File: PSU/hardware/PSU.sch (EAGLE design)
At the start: 211 parts, among them J1 SWD, J2 UART, Q1 PMOS-DPAK, Q10 PMOS-SOT23, Q11 NPN, Q12 PMOS-SOT23, Q13 NPN, Q14 NPN, Q15 PMOS-SOT23, Q2 PMOS-SOT23, Q3 NPN, Q4 PMOS-SOT23, Q5 NMOS-SOT23, Q6 PMOS-DPAK, Q7 PMOS-SOT23, Q8 NMOS-SOT23, Q9 PMOS-DPAK, U1 LM2576, U10 4069, U11 LTV-247, U12 74HC08, U13 STM8S003K3T6C, U14 74HC08, U15 4051, U16 358, U17 358, U18 74HC32, U2 MT3608, U3 7805, U4 324, U5 MC34063, U6 MT3608, U7 LM2576, U8 MC34063, U9 TP4056

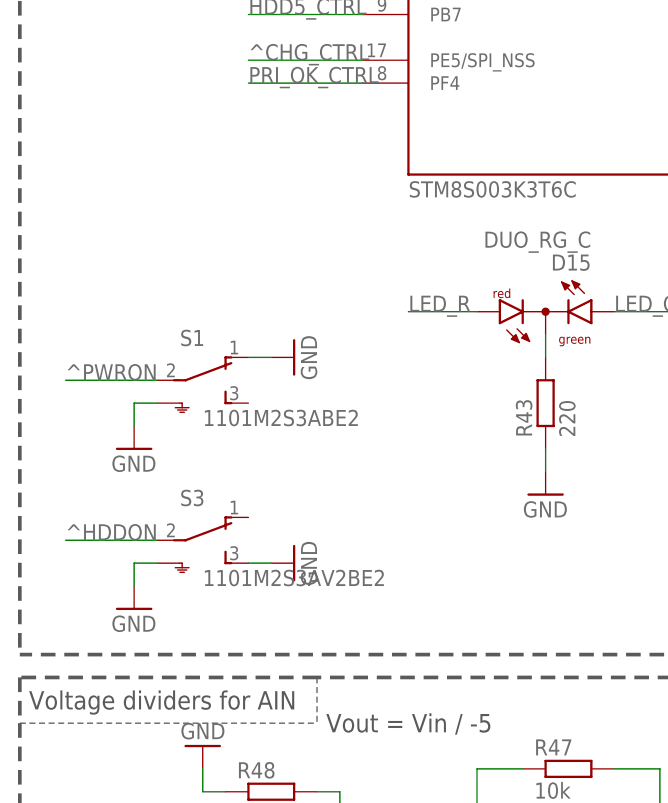
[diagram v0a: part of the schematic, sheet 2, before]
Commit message: [HW/PSU] Add switch debouncing
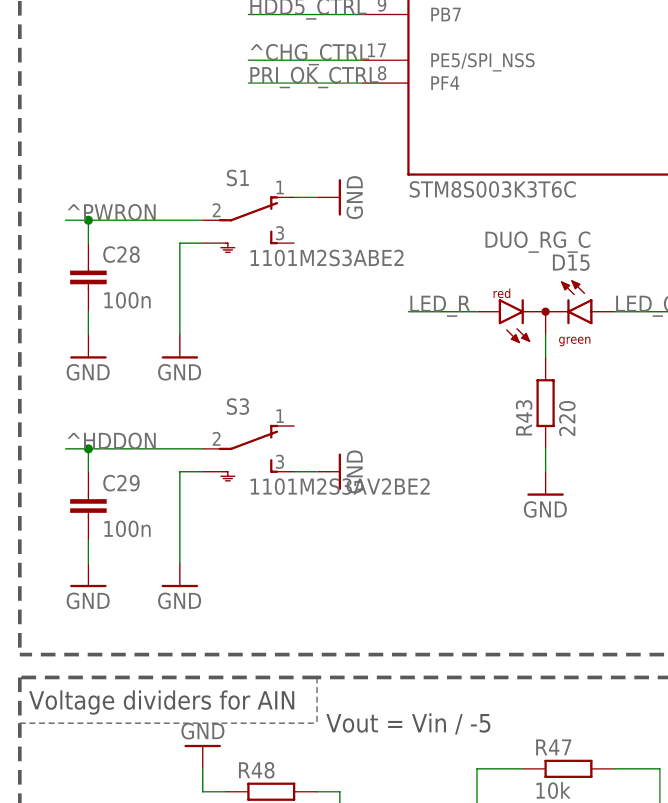
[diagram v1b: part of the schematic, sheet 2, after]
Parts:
- added C28, C29: 100n, rcl:C-EUC0805
- added R82: 100k, rcl:R-EU_R0805
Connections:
- net GND: now also C28.2, C29.2, R82.1
- net VBACKUP: now also R82.2
- net ^HDDON: now also C29.1
- net ^PWRON: now also C28.1
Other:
- moved on the sheet: S1, S3
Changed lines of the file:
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@@
 <part name="R81" library="rcl" library_urn="urn:adsk.eagle:library:334" deviceset="R-EU_" device="R0805" package3d_urn="urn:adsk.eagle:package:23553/2" value="10k"/>
 <part name="P+9" library="supply1" library_urn="urn:adsk.eagle:library:371" deviceset="+5V" device=""/>
+<part name="R82" library="rcl" library_urn="urn:adsk.eagle:library:334" deviceset="R-EU_" device="R0805" package3d_urn="urn:adsk.eagle:package:23553/2" value="100k"/>
+<part name="GND3" library="supply1" library_urn="urn:adsk.eagle:library:371" deviceset="GND" device=""/>
+<part name="C28" library="rcl" library_urn="urn:adsk.eagle:library:334" deviceset="C-EU" device="C0805" package3d_urn="urn:adsk.eagle:package:23617/2" value="100n"/>
+<part name="GND4" library="supply1" library_urn="urn:adsk.eagle:library:371" deviceset="GND" device=""/>
+<part name="C29" library="rcl" library_urn="urn:adsk.eagle:library:334" deviceset="C-EU" device="C0805" package3d_urn="urn:adsk.eagle:package:23617/2" value="100n"/>
+<part name="GND8" library="supply1" library_urn="urn:adsk.eagle:library:371" deviceset="GND" device=""/>
 </parts>
 <sheets>
@@
 <attribute name="VALUE" x="364.363" y="46.2026" size="1.778" layer="96"/>
 </instance>
-<instance part="GND55" gate="1" x="363.22" y="40.64" smashed="yes">
-<attribute name="VALUE" x="360.68" y="38.1" size="1.778" layer="96"/>
+<instance part="GND55" gate="1" x="363.22" y="38.1" smashed="yes">
+<attribute name="VALUE" x="360.68" y="35.56" size="1.778" layer="96"/>
 </instance>
 <instance part="R31" gate="G$1" x="317.5" y="48.26" smashed="yes" rot="R90">
@@
 <attribute name="VALUE" x="314.96" y="35.56" size="1.778" layer="96" font="vector" rot="MR180"/>
 </instance>
+<instance part="R82" gate="G$1" x="373.38" y="48.26" smashed="yes" rot="R90">
+<attribute name="NAME" x="371.8814" y="44.45" size="1.778" layer="95" rot="R90"/>
+<attribute name="VALUE" x="376.682" y="44.45" size="1.778" layer="96" rot="R90"/>
+</instance>
+<instance part="GND3" gate="1" x="373.38" y="38.1" smashed="yes">
+<attribute name="VALUE" x="370.84" y="35.56" size="1.778" layer="96"/>
+</instance>
 </instances>
 <busses>
@@
 <segment>
 <pinref part="C22" gate="G$1" pin="2"/>
-<wire x1="363.22" y1="45.72" x2="363.22" y2="43.18" width="0.1524" layer="91"/>
+<wire x1="363.22" y1="45.72" x2="363.22" y2="40.64" width="0.1524" layer="91"/>
 <pinref part="GND55" gate="1" pin="GND"/>
 </segment>
@@
 <pinref part="GND2" gate="1" pin="GND"/>
 </segment>
+<segment>
+<pinref part="R82" gate="G$1" pin="1"/>
+<wire x1="373.38" y1="43.18" x2="373.38" y2="40.64" width="0.1524" layer="91"/>
+<pinref part="GND3" gate="1" pin="GND"/>
+</segment>
 </net>
 <net name="+5V_LOGIC" class="3">
@@
 <pinref part="U9" gate="G$1" pin="BAT"/>
 <wire x1="360.68" y1="55.88" x2="363.22" y2="55.88" width="0.1524" layer="91"/>
-<label x="365.76" y="55.88" size="1.778" layer="95" xref="yes"/>
+<label x="365.76" y="55.88" size="1.778" layer="95"/>
 <pinref part="C22" gate="G$1" pin="1"/>
-<wire x1="363.22" y1="55.88" x2="365.76" y2="55.88" width="0.1524" layer="91"/>
 <wire x1="363.22" y1="55.88" x2="363.22" y2="53.34" width="0.1524" layer="91"/>
 <junction x="363.22" y="55.88"/>
+<wire x1="363.22" y1="55.88" x2="373.38" y2="55.88" width="0.1524" layer="91"/>
+<pinref part="R82" gate="G$1" pin="2"/>
+<wire x1="373.38" y1="55.88" x2="373.38" y2="53.34" width="0.1524" layer="91"/>
 </segment>
 <segment>
@@
 <attribute name="VALUE" x="345.44" y="185.42" size="1.778" layer="96"/>
 </instance>
-<instance part="S1" gate="G$1" x="27.94" y="160.02" smashed="yes">
-<attribute name="NAME" x="25.4" y="163.83" size="1.778" layer="95"/>
-<attribute name="VALUE" x="27.94" y="154.94" size="1.778" layer="96"/>
-</instance>
-<instance part="S3" gate="G$1" x="27.94" y="142.24" smashed="yes">
-<attribute name="NAME" x="25.4" y="146.05" size="1.778" layer="95"/>
-<attribute name="VALUE" x="27.94" y="137.16" size="1.778" layer="96"/>
+<instance part="S1" gate="G$1" x="33.02" y="177.8" smashed="yes">
+<attribute name="NAME" x="30.48" y="181.61" size="1.778" layer="95"/>
+<attribute name="VALUE" x="33.02" y="172.72" size="1.778" layer="96"/>
+</instance>
+<instance part="S3" gate="G$1" x="33.02" y="152.4" smashed="yes">
+<attribute name="NAME" x="30.48" y="156.21" size="1.778" layer="95"/>
+<attribute name="VALUE" x="33.02" y="147.32" size="1.778" layer="96"/>
 </instance>
-<instance part="GND7" gate="1" x="20.32" y="152.4" smashed="yes">
-<attribute name="VALUE" x="17.78" y="149.86" size="1.778" layer="96"/>
+<instance part="GND7" gate="1" x="25.4" y="162.56" smashed="yes">
+<attribute name="VALUE" x="22.86" y="160.02" size="1.778" layer="96"/>
 </instance>
-<instance part="GND10" gate="1" x="20.32" y="134.62" smashed="yes">
-<attribute name="VALUE" x="17.78" y="132.08" size="1.778" layer="96"/>
+<instance part="GND10" gate="1" x="25.4" y="137.16" smashed="yes">
+<attribute name="VALUE" x="22.86" y="134.62" size="1.778" layer="96"/>
 </instance>
 <instance part="VCC1" gate="G$1" x="370.84" y="213.36" smashed="yes">
@@
 <attribute name="VALUE" x="63.5" y="144.78" size="1.778" layer="96"/>
 </instance>
-<instance part="GND70" gate="1" x="38.1" y="162.56" smashed="yes" rot="R90">
-<attribute name="VALUE" x="40.64" y="160.02" size="1.778" layer="96" rot="R90"/>
+<instance part="GND70" gate="1" x="43.18" y="180.34" smashed="yes" rot="R90">
+<attribute name="VALUE" x="45.72" y="177.8" size="1.778" layer="96" rot="R90"/>
 </instance>
-<instance part="GND71" gate="1" x="38.1" y="139.7" smashed="yes" rot="R90">
-<attribute name="VALUE" x="40.64" y="137.16" size="1.778" layer="96" rot="R90"/>
+<instance part="GND71" gate="1" x="43.18" y="149.86" smashed="yes" rot="R90">
+<attribute name="VALUE" x="45.72" y="147.32" size="1.778" layer="96" rot="R90"/>
 </instance>
 <instance part="U15" gate="A" x="121.92" y="152.4" smashed="yes">
@@
 <attribute name="VALUE" x="360.68" y="81.28" size="1.778" layer="96" rot="R90"/>
 </instance>
+<instance part="C28" gate="G$1" x="15.24" y="172.72" smashed="yes">
+<attribute name="NAME" x="16.764" y="173.101" size="1.778" layer="95"/>
+<attribute name="VALUE" x="16.764" y="168.021" size="1.778" layer="96"/>
+</instance>
+<instance part="GND4" gate="1" x="15.24" y="162.56" smashed="yes">
+<attribute name="VALUE" x="12.7" y="160.02" size="1.778" layer="96"/>
+</instance>
+<instance part="C29" gate="G$1" x="15.24" y="147.32" smashed="yes">
+<attribute name="NAME" x="16.764" y="147.701" size="1.778" layer="95"/>
+<attribute name="VALUE" x="16.764" y="142.621" size="1.778" layer="96"/>
+</instance>
+<instance part="GND8" gate="1" x="15.24" y="137.16" smashed="yes">
+<attribute name="VALUE" x="12.7" y="134.62" size="1.778" layer="96"/>
+</instance>
 </instances>
 <busses>
@@
 <segment>
 <pinref part="GND7" gate="1" pin="GND"/>
-<wire x1="20.32" y1="154.94" x2="20.32" y2="157.48" width="0.1524" layer="91"/>
+<wire x1="25.4" y1="165.1" x2="25.4" y2="175.26" width="0.1524" layer="91"/>
 <pinref part="S1" gate="G$1" pin="SH"/>
-<wire x1="20.32" y1="157.48" x2="22.86" y2="157.48" width="0.1524" layer="91"/>
+<wire x1="25.4" y1="175.26" x2="27.94" y2="175.26" width="0.1524" layer="91"/>
 </segment>
 <segment>
 <pinref part="GND10" gate="1" pin="GND"/>
-<wire x1="20.32" y1="137.16" x2="20.32" y2="139.7" width="0.1524" layer="91"/>
+<wire x1="25.4" y1="139.7" x2="25.4" y2="149.86" width="0.1524" layer="91"/>
 <pinref part="S3" gate="G$1" pin="SH"/>
-<wire x1="20.32" y1="139.7" x2="22.86" y2="139.7" width="0.1524" layer="91"/>
+<wire x1="25.4" y1="149.86" x2="27.94" y2="149.86" width="0.1524" layer="91"/>
 </segment>
 <segment>
@@
 <segment>
 <pinref part="S1" gate="G$1" pin="O"/>
-<wire x1="33.02" y1="162.56" x2="35.56" y2="162.56" width="0.1524" layer="91"/>
+<wire x1="38.1" y1="180.34" x2="40.64" y2="180.34" width="0.1524" layer="91"/>
 <pinref part="GND70" gate="1" pin="GND"/>
 </segment>
 <segment>
 <pinref part="S3" gate="G$1" pin="S"/>
-<wire x1="33.02" y1="139.7" x2="35.56" y2="139.7" width="0.1524" layer="91"/>
+<wire x1="38.1" y1="149.86" x2="40.64" y2="149.86" width="0.1524" layer="91"/>
 <pinref part="GND71" gate="1" pin="GND"/>
 </segment>
@@
 <pinref part="GND101" gate="1" pin="GND"/>
 </segment>
+<segment>
+<pinref part="C28" gate="G$1" pin="2"/>
+<wire x1="15.24" y1="167.64" x2="15.24" y2="165.1" width="0.1524" layer="91"/>
+<pinref part="GND4" gate="1" pin="GND"/>
+</segment>
+<segment>
+<pinref part="C29" gate="G$1" pin="2"/>
+<wire x1="15.24" y1="142.24" x2="15.24" y2="139.7" width="0.1524" layer="91"/>
+<pinref part="GND8" gate="1" pin="GND"/>
+</segment>
 </net>
 <net name="VCAP" class="1">
@@
 <segment>
 <pinref part="S1" gate="G$1" pin="P"/>
-<label x="12.7" y="160.02" size="1.778" layer="95"/>
-<wire x1="22.86" y1="160.02" x2="12.7" y2="160.02" width="0.1524" layer="91"/>
+<label x="12.7" y="177.8" size="1.778" layer="95"/>
+<wire x1="27.94" y1="177.8" x2="15.24" y2="177.8" width="0.1524" layer="91"/>
+<pinref part="C28" gate="G$1" pin="1"/>
+<wire x1="15.24" y1="177.8" x2="12.7" y2="177.8" width="0.1524" layer="91"/>
+<wire x1="15.24" y1="175.26" x2="15.24" y2="177.8" width="0.1524" layer="91"/>
+<junction x="15.24" y="177.8"/>
 </segment>
 <segment>
@@
 <segment>
 <pinref part="S3" gate="G$1" pin="P"/>
-<label x="12.7" y="142.24" size="1.778" layer="95"/>
-<wire x1="22.86" y1="142.24" x2="12.7" y2="142.24" width="0.1524" layer="91"/>
+<label x="12.7" y="152.4" size="1.778" layer="95"/>
+<wire x1="27.94" y1="152.4" x2="15.24" y2="152.4" width="0.1524" layer="91"/>
+<pinref part="C29" gate="G$1" pin="1"/>
+<wire x1="15.24" y1="152.4" x2="12.7" y2="152.4" width="0.1524" layer="91"/>
+<wire x1="15.24" y1="149.86" x2="15.24" y2="152.4" width="0.1524" layer="91"/>
+<junction x="15.24" y="152.4"/>
 </segment>
 <segment>

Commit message: [HW/PSU] Correct resistor values
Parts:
- R1: value 10k -> 47k
- R12: value 2.2k -> 330
- R3: value 3.3k -> 15k
- R64: value 2.2k -> 9.1k
- R68: value 6.8k -> 30k
- R77, R79: value 10k -> 100k
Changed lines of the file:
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@@
 <part name="GND24" library="supply1" library_urn="urn:adsk.eagle:library:371" deviceset="GND" device=""/>
 <part name="D1" library="custom" deviceset="SS*" device="34" value="SS34"/>
-<part name="R1" library="rcl" library_urn="urn:adsk.eagle:library:334" deviceset="R-EU_" device="R0805" package3d_urn="urn:adsk.eagle:package:23553/2" value="10k"/>
-<part name="R3" library="rcl" library_urn="urn:adsk.eagle:library:334" deviceset="R-EU_" device="R0805" package3d_urn="urn:adsk.eagle:package:23553/2" value="3.3k"/>
+<part name="R1" library="rcl" library_urn="urn:adsk.eagle:library:334" deviceset="R-EU_" device="R0805" package3d_urn="urn:adsk.eagle:package:23553/2" value="47k"/>
+<part name="R3" library="rcl" library_urn="urn:adsk.eagle:library:334" deviceset="R-EU_" device="R0805" package3d_urn="urn:adsk.eagle:package:23553/2" value="15k"/>
 <part name="GND25" library="supply1" library_urn="urn:adsk.eagle:library:371" deviceset="GND" device=""/>
 <part name="GND26" library="supply1" library_urn="urn:adsk.eagle:library:371" deviceset="GND" device=""/>
@@
 <part name="R57" library="rcl" library_urn="urn:adsk.eagle:library:334" deviceset="R-EU_" device="R0805" package3d_urn="urn:adsk.eagle:package:23553/2" value="1k"/>
 <part name="R62" library="rcl" library_urn="urn:adsk.eagle:library:334" deviceset="R-EU_" device="R0805" package3d_urn="urn:adsk.eagle:package:23553/2" value="3.3k"/>
-<part name="R64" library="rcl" library_urn="urn:adsk.eagle:library:334" deviceset="R-EU_" device="R0805" package3d_urn="urn:adsk.eagle:package:23553/2" value="2.2k"/>
-<part name="R68" library="rcl" library_urn="urn:adsk.eagle:library:334" deviceset="R-EU_" device="R0805" package3d_urn="urn:adsk.eagle:package:23553/2" value="6.8k"/>
+<part name="R64" library="rcl" library_urn="urn:adsk.eagle:library:334" deviceset="R-EU_" device="R0805" package3d_urn="urn:adsk.eagle:package:23553/2" value="9.1k"/>
+<part name="R68" library="rcl" library_urn="urn:adsk.eagle:library:334" deviceset="R-EU_" device="R0805" package3d_urn="urn:adsk.eagle:package:23553/2" value="30k"/>
 <part name="P+3" library="supply1" library_urn="urn:adsk.eagle:library:371" deviceset="+5V" device=""/>
 <part name="P-1" library="T1200" deviceset="-22V" device=""/>
@@
 <part name="R69" library="rcl" library_urn="urn:adsk.eagle:library:334" deviceset="R-EU_" device="R0805" package3d_urn="urn:adsk.eagle:package:23553/2" value="1k"/>
 <part name="JP1" library="jumper" library_urn="urn:adsk.eagle:library:252" deviceset="JP1Q" device="" package3d_urn="urn:adsk.eagle:package:15455/1" value="LedChg"/>
-<part name="R12" library="rcl" library_urn="urn:adsk.eagle:library:334" deviceset="R-EU_" device="R0805" package3d_urn="urn:adsk.eagle:package:23553/2" value="2.2k"/>
+<part name="R12" library="rcl" library_urn="urn:adsk.eagle:library:334" deviceset="R-EU_" device="R0805" package3d_urn="urn:adsk.eagle:package:23553/2" value="330"/>
 <part name="Q11" library="SparkFun-DiscreteSemi" deviceset="TRANS_NPN" device="-MMBT2222AL" value="NPN"/>
 <part name="R39" library="rcl" library_urn="urn:adsk.eagle:library:334" deviceset="R-EU_" device="R0805" package3d_urn="urn:adsk.eagle:package:23553/2" value="10k"/>
@@
 <part name="Q13" library="SparkFun-DiscreteSemi" deviceset="TRANS_NPN" device="-MMBT2222AL" value="NPN"/>
 <part name="GND1" library="supply1" library_urn="urn:adsk.eagle:library:371" deviceset="GND" device=""/>
-<part name="R77" library="rcl" library_urn="urn:adsk.eagle:library:334" deviceset="R-EU_" device="R0805" package3d_urn="urn:adsk.eagle:package:23553/2" value="10k"/>
+<part name="R77" library="rcl" library_urn="urn:adsk.eagle:library:334" deviceset="R-EU_" device="R0805" package3d_urn="urn:adsk.eagle:package:23553/2" value="100k"/>
 <part name="R78" library="rcl" library_urn="urn:adsk.eagle:library:334" deviceset="R-EU_" device="R0805" package3d_urn="urn:adsk.eagle:package:23553/2" value="10k"/>
 <part name="Q14" library="SparkFun-DiscreteSemi" deviceset="TRANS_NPN" device="-MMBT2222AL" value="NPN"/>
 <part name="R80" library="rcl" library_urn="urn:adsk.eagle:library:334" deviceset="R-EU_" device="R0805" package3d_urn="urn:adsk.eagle:package:23553/2" value="10k"/>
-<part name="R79" library="rcl" library_urn="urn:adsk.eagle:library:334" deviceset="R-EU_" device="R0805" package3d_urn="urn:adsk.eagle:package:23553/2" value="10k"/>
+<part name="R79" library="rcl" library_urn="urn:adsk.eagle:library:334" deviceset="R-EU_" device="R0805" package3d_urn="urn:adsk.eagle:package:23553/2" value="100k"/>
 <part name="GND2" library="supply1" library_urn="urn:adsk.eagle:library:371" deviceset="GND" device=""/>
 <part name="TP21" library="testpad" library_urn="urn:adsk.eagle:library:385" deviceset="TP" device="B1,27" package3d_urn="urn:adsk.eagle:package:27944/2"/>

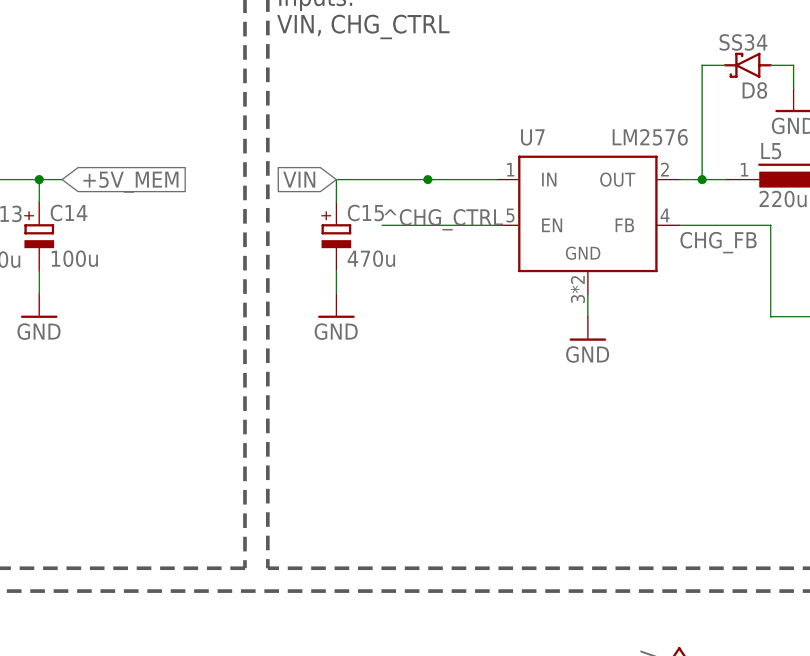
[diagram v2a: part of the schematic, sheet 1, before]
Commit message: [HW/PSU] Fix Vbat to Vin voltage leak
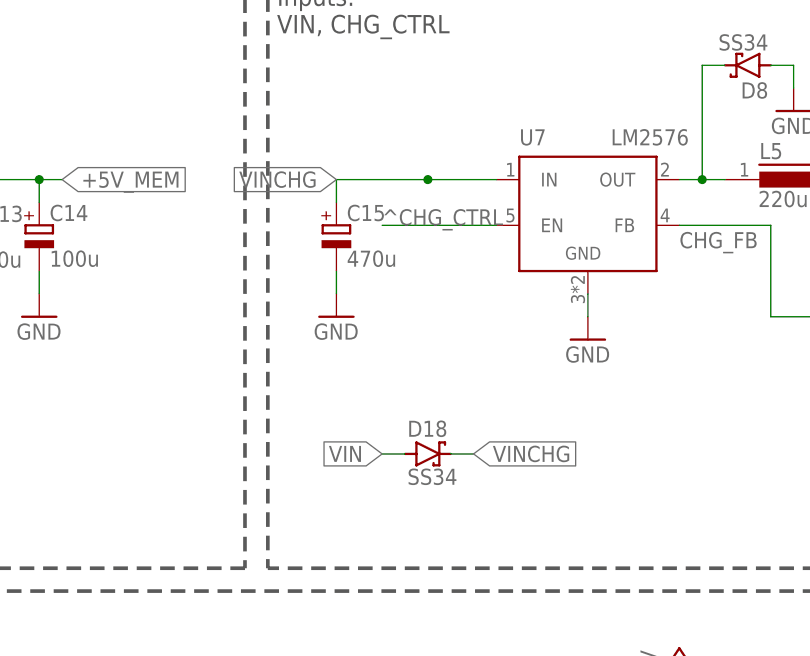
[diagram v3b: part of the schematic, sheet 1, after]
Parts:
- added D18: SS34, custom:SS34
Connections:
- new net VINCHG: C15.+, D18.C, U7.IN
- net VIN: now also D18.A; no longer C15.+, U7.IN
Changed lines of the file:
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@@
 <part name="C29" library="rcl" library_urn="urn:adsk.eagle:library:334" deviceset="C-EU" device="C0805" package3d_urn="urn:adsk.eagle:package:23617/2" value="100n"/>
 <part name="GND8" library="supply1" library_urn="urn:adsk.eagle:library:371" deviceset="GND" device=""/>
+<part name="D18" library="custom" deviceset="SS*" device="34" value="SS34"/>
 </parts>
 <sheets>
@@
 <attribute name="VALUE" x="370.84" y="35.56" size="1.778" layer="96"/>
 </instance>
+<instance part="D18" gate="G$1" x="139.7" y="96.52" smashed="yes">
+<attribute name="NAME" x="137.414" y="98.425" size="1.778" layer="95"/>
+<attribute name="VALUE" x="137.414" y="93.091" size="1.778" layer="96"/>
+</instance>
 </instances>
 <busses>
@@
 <net name="VIN" class="0">
 <segment>
-<pinref part="C15" gate="G$1" pin="+"/>
-<wire x1="129.54" y1="124.46" x2="129.54" y2="127" width="0.1524" layer="91"/>
-<pinref part="U7" gate="NC1" pin="IN"/>
-<wire x1="139.7" y1="127" x2="147.32" y2="127" width="0.1524" layer="91"/>
-<label x="129.54" y="127" size="1.778" layer="95" rot="R180" xref="yes"/>
-<wire x1="139.7" y1="127" x2="129.54" y2="127" width="0.1524" layer="91"/>
-<junction x="139.7" y="127"/>
-</segment>
-<segment>
 <pinref part="D2" gate="G$1" pin="A"/>
 <wire x1="147.32" y1="220.98" x2="144.78" y2="220.98" width="0.1524" layer="91"/>
@@
 <label x="88.9" y="180.34" size="1.778" layer="95" xref="yes"/>
 <pinref part="R8" gate="G$1" pin="2"/>
+</segment>
+<segment>
+<pinref part="D18" gate="G$1" pin="A"/>
+<wire x1="137.16" y1="96.52" x2="134.62" y2="96.52" width="0.1524" layer="91"/>
+<label x="134.62" y="96.52" size="1.778" layer="95" rot="R180" xref="yes"/>
 </segment>
 </net>
@@
 </segment>
 </net>
+<net name="VINCHG" class="0">
+<segment>
+<pinref part="C15" gate="G$1" pin="+"/>
+<wire x1="129.54" y1="124.46" x2="129.54" y2="127" width="0.1524" layer="91"/>
+<pinref part="U7" gate="NC1" pin="IN"/>
+<wire x1="139.7" y1="127" x2="147.32" y2="127" width="0.1524" layer="91"/>
+<label x="129.54" y="127" size="1.778" layer="95" rot="R180" xref="yes"/>
+<wire x1="139.7" y1="127" x2="129.54" y2="127" width="0.1524" layer="91"/>
+<junction x="139.7" y="127"/>
+</segment>
+<segment>
+<pinref part="D18" gate="G$1" pin="C"/>
+<wire x1="142.24" y1="96.52" x2="144.78" y2="96.52" width="0.1524" layer="91"/>
+<label x="144.78" y="96.52" size="1.778" layer="95" xref="yes"/>
+</segment>
+</net>
